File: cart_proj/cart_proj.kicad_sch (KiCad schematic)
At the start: 9 parts, among them CON1 GENESIS-EDGE, J1 PAD3, J2 PAD4, U1 PAL16R4, U2 74LS244, U3 74LS244, U4 27C800

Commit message: Add picture
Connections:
- net ~{XCVR2_OE}: now also U1.19 (IO1)
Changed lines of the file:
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@@
     (effects (font (size 1.27 1.27)) (justify left bottom))
+  )
+  (label "~{XCVR2_OE}" (at 82.55 26.67 180) (fields_autoplaced)
+    (effects (font (size 1.27 1.27)) (justify right bottom))
   )
   (label "A21" (at 278.13 64.77 180) (fields_autoplaced)

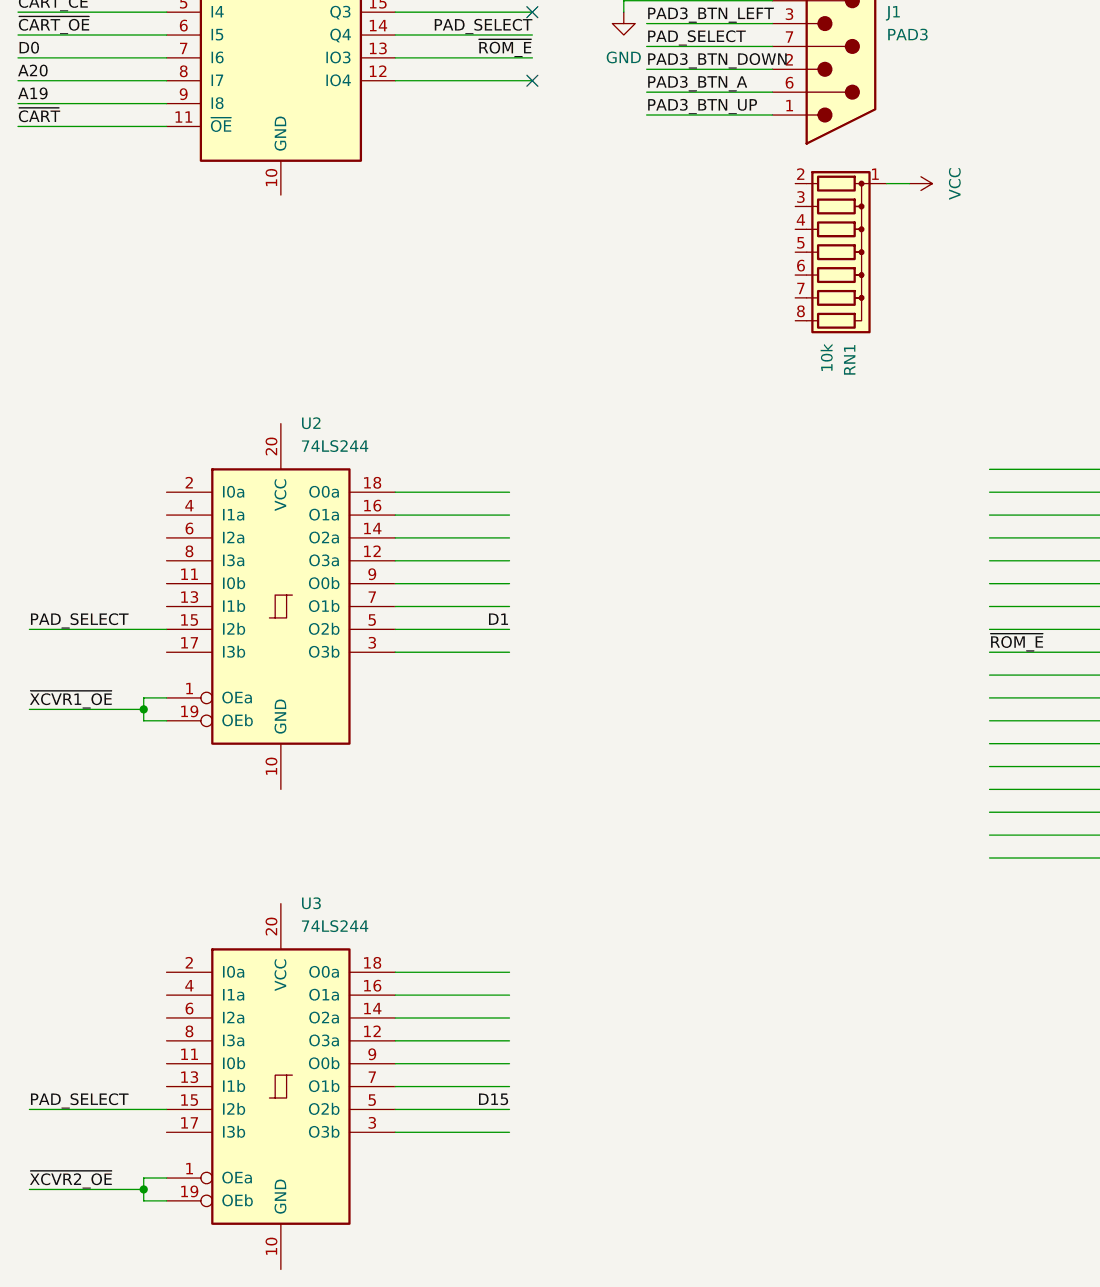
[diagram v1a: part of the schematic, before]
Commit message: Additional connections on first 74LS244
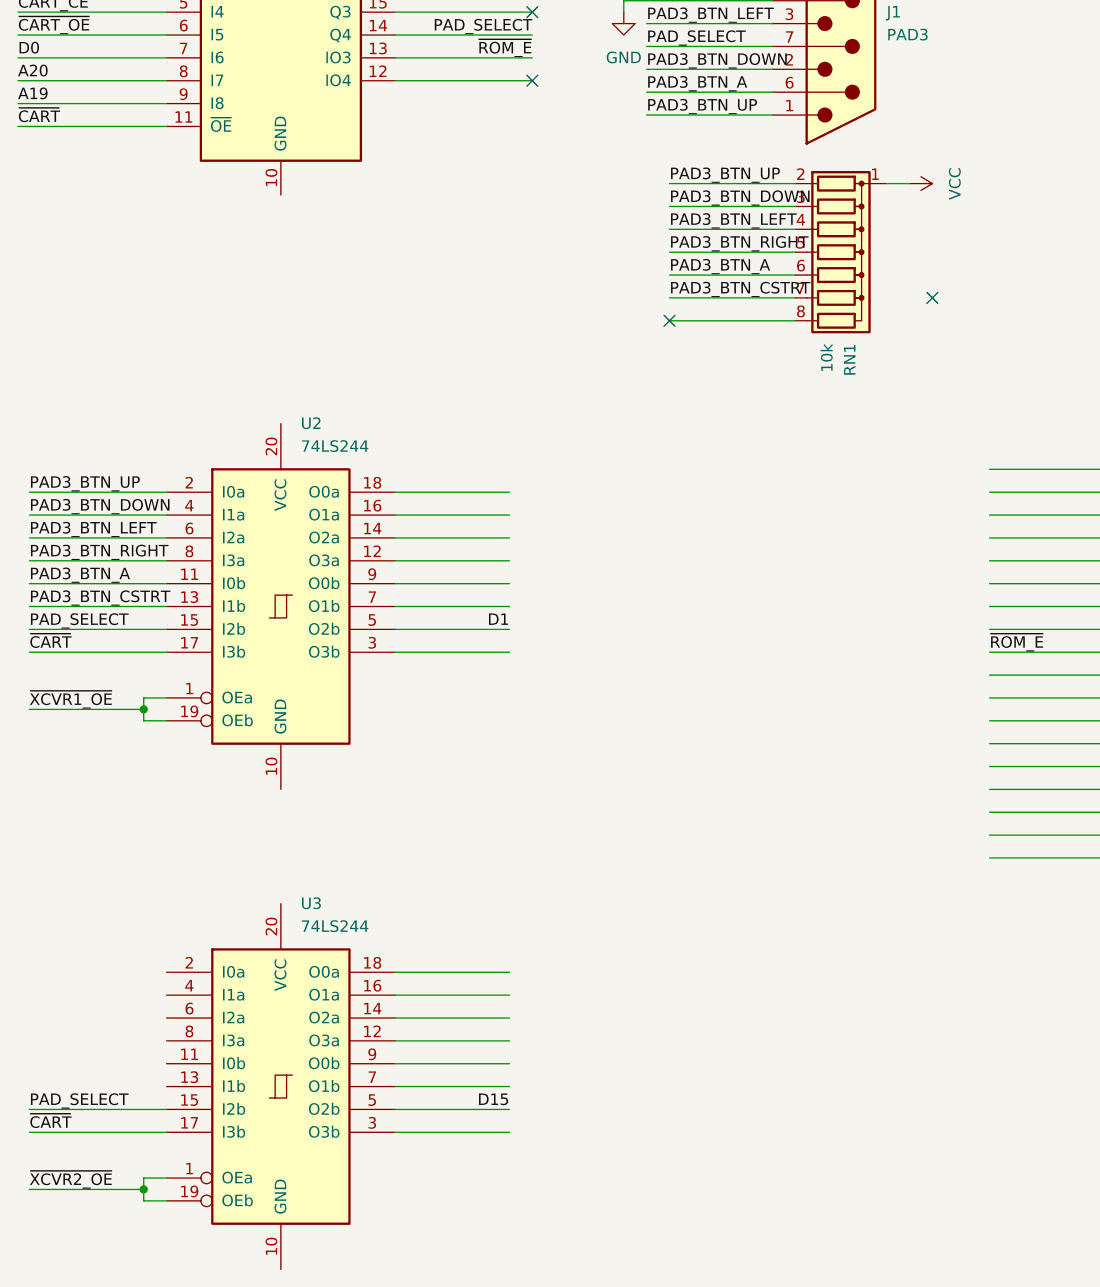
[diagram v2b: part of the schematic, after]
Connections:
- net PAD3_BTN_A: now also RN1.6 (R5), U2.11 (I0b)
- net PAD3_BTN_CSTRT: now also RN1.7 (R6), U2.13 (I1b)
- net PAD3_BTN_DOWN: now also RN1.3 (R2), U2.4 (I1a)
- net PAD3_BTN_LEFT: now also RN1.4 (R3), U2.6 (I2a)
- net PAD3_BTN_RIGHT: now also RN1.5 (R4), U2.8 (I3a)
- net PAD3_BTN_UP: now also RN1.2 (R1), U2.2 (I0a)
- net ~{CART}: now also U2.17 (I3b), U3.17 (I3b)
- no-connect marks 4 -> 6
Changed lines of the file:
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@@
   (junction (at 39.37 167.64) (diameter 0) (color 0 0 0 0)
   )
+  (no_connect (at 127 68.58))
   (no_connect (at 82.55 34.29))
   (no_connect (at 82.55 31.75))
   (no_connect (at 82.55 44.45))
+  (no_connect (at 97.79 71.12))
   (no_connect (at 82.55 36.83))
   (wire (pts (xy 95.25 33.02) (xy 109.22 33.02))
@@
     (stroke (width 0) (type default))
   )
+  (wire (pts (xy 26.67 100.33) (xy 41.91 100.33))
+    (stroke (width 0) (type default))
+  )
   (wire (pts (xy 67.31 41.91) (xy 82.55 41.91))
     (stroke (width 0) (type default))
@@
     (stroke (width 0) (type default))
   )
+  (wire (pts (xy 97.79 68.58) (xy 111.76 68.58))
+    (stroke (width 0) (type default))
+  )
   (wire (pts (xy 260.35 44.45) (xy 278.13 44.45))
     (stroke (width 0) (type default))
   )
+  (wire (pts (xy 26.67 95.25) (xy 41.91 95.25))
+    (stroke (width 0) (type default))
+  )
   (wire (pts (xy 260.35 49.53) (xy 278.13 49.53))
     (stroke (width 0) (type default))
@@
     (stroke (width 0) (type default))
   )
+  (wire (pts (xy 26.67 102.87) (xy 41.91 102.87))
+    (stroke (width 0) (type default))
+  )
   (wire (pts (xy 212.09 80.01) (xy 232.41 80.01))
     (stroke (width 0) (type default))
   )
+  (wire (pts (xy 97.79 60.96) (xy 111.76 60.96))
+    (stroke (width 0) (type default))
+  )
   (wire (pts (xy 92.71 27.94) (xy 109.22 27.94))
     (stroke (width 0) (type default))
@@
     (stroke (width 0) (type default))
   )
+  (wire (pts (xy 97.79 63.5) (xy 111.76 63.5))
+    (stroke (width 0) (type default))
+  )
   (wire (pts (xy 212.09 100.33) (xy 232.41 100.33))
     (stroke (width 0) (type default))
@@
     (stroke (width 0) (type default))
   )
+  (wire (pts (xy 97.79 66.04) (xy 111.76 66.04))
+    (stroke (width 0) (type default))
+  )
   (wire (pts (xy 41.91 105.41) (xy 26.67 105.41))
     (stroke (width 0) (type default))
@@
     (stroke (width 0) (type default))
   )
+  (wire (pts (xy 97.79 71.12) (xy 111.76 71.12))
+    (stroke (width 0) (type default))
+  )
+  (wire (pts (xy 26.67 90.17) (xy 41.91 90.17))
+    (stroke (width 0) (type default))
+  )
   (wire (pts (xy 67.31 31.75) (xy 82.55 31.75))
     (stroke (width 0) (type default))
@@
     (stroke (width 0) (type default))
   )
+  (wire (pts (xy 97.79 58.42) (xy 111.76 58.42))
+    (stroke (width 0) (type default))
+  )
+  (wire (pts (xy 97.79 55.88) (xy 111.76 55.88))
+    (stroke (width 0) (type default))
+  )
   (wire (pts (xy 133.35 92.71) (xy 149.86 92.71))
     (stroke (width 0) (type default))
@@
     (stroke (width 0) (type default))
   )
+  (wire (pts (xy 26.67 161.29) (xy 41.91 161.29))
+    (stroke (width 0) (type default))
+  )
   (wire (pts (xy 39.37 115.57) (xy 41.91 115.57))
     (stroke (width 0) (type default))
@@
     (stroke (width 0) (type default))
   )
+  (wire (pts (xy 26.67 92.71) (xy 41.91 92.71))
+    (stroke (width 0) (type default))
+  )
   (wire (pts (xy 133.35 125.73) (xy 149.86 125.73))
     (stroke (width 0) (type default))
@@
     (stroke (width 0) (type default))
   )
+  (wire (pts (xy 26.67 107.95) (xy 41.91 107.95))
+    (stroke (width 0) (type default))
+  )
   (wire (pts (xy 260.35 97.79) (xy 278.13 97.79))
     (stroke (width 0) (type default))
@@
     (stroke (width 0) (type default))
   )
+  (wire (pts (xy 26.67 97.79) (xy 41.91 97.79))
+    (stroke (width 0) (type default))
+  )
   (wire (pts (xy 260.35 110.49) (xy 278.13 110.49))
     (stroke (width 0) (type default))
@@
     (effects (font (size 1.27 1.27)) (justify left bottom))
   )
+  (label "PAD3_BTN_A" (at 97.79 66.04 0) (fields_autoplaced)
+    (effects (font (size 1.27 1.27)) (justify left bottom))
+  )
   (label "~{ROM_E}" (at 82.55 41.91 180) (fields_autoplaced)
     (effects (font (size 1.27 1.27)) (justify right bottom))
@@
     (effects (font (size 1.27 1.27)) (justify right bottom))
   )
+  (label "PAD3_BTN_LEFT" (at 97.79 60.96 0) (fields_autoplaced)
+    (effects (font (size 1.27 1.27)) (justify left bottom))
+  )
   (label "PAD4_BTN_UP" (at 154.94 48.26 0) (fields_autoplaced)
     (effects (font (size 1.27 1.27)) (justify left bottom))
@@
     (effects (font (size 1.27 1.27)) (justify left bottom))
   )
+  (label "PAD3_BTN_CSTRT" (at 97.79 68.58 0) (fields_autoplaced)
+    (effects (font (size 1.27 1.27)) (justify left bottom))
+  )
   (label "PAD4_BTN_A" (at 154.94 45.72 0) (fields_autoplaced)
     (effects (font (size 1.27 1.27)) (justify left bottom))
@@
     (effects (font (size 1.27 1.27)) (justify left bottom))
   )
+  (label "~{CART}" (at 26.67 107.95 0) (fields_autoplaced)
+    (effects (font (size 1.27 1.27)) (justify left bottom))
+  )
   (label "PAD4_BTN_DOWN" (at 154.94 43.18 0) (fields_autoplaced)
     (effects (font (size 1.27 1.27)) (justify left bottom))
@@
     (effects (font (size 1.27 1.27)) (justify right bottom))
   )
+  (label "PAD3_BTN_RIGHT" (at 26.67 97.79 0) (fields_autoplaced)
+    (effects (font (size 1.27 1.27)) (justify left bottom))
+  )
   (label "VCLK" (at 278.13 90.17 180) (fields_autoplaced)
     (effects (font (size 1.27 1.27)) (justify right bottom))
@@
     (effects (font (size 1.27 1.27)) (justify left bottom))
   )
+  (label "PAD3_BTN_DOWN" (at 26.67 92.71 0) (fields_autoplaced)
+    (effects (font (size 1.27 1.27)) (justify left bottom))
+  )
   (label "PAD3_BTN_DOWN" (at 95.25 43.18 0) (fields_autoplaced)
     (effects (font (size 1.27 1.27)) (justify left bottom))
   )
+  (label "PAD3_BTN_A" (at 26.67 100.33 0) (fields_autoplaced)
+    (effects (font (size 1.27 1.27)) (justify left bottom))
+  )
   (label "PAD3_BTN_LEFT" (at 95.25 38.1 0) (fields_autoplaced)
     (effects (font (size 1.27 1.27)) (justify left bottom))
@@
     (effects (font (size 1.27 1.27)) (justify right bottom))
   )
+  (label "PAD3_BTN_UP" (at 97.79 55.88 0) (fields_autoplaced)
+    (effects (font (size 1.27 1.27)) (justify left bottom))
+  )
+  (label "PAD3_BTN_UP" (at 26.67 90.17 0) (fields_autoplaced)
+    (effects (font (size 1.27 1.27)) (justify left bottom))
+  )
   (label "PAD_SELECT" (at 82.55 39.37 180) (fields_autoplaced)
     (effects (font (size 1.27 1.27)) (justify right bottom))
@@
     (effects (font (size 1.27 1.27)) (justify right bottom))
   )
+  (label "~{CART}" (at 26.67 161.29 0) (fields_autoplaced)
+    (effects (font (size 1.27 1.27)) (justify left bottom))
+  )
   (label "D1" (at 80.01 105.41 180) (fields_autoplaced)
     (effects (font (size 1.27 1.27)) (justify right bottom))
@@
     (effects (font (size 1.27 1.27)) (justify right bottom))
   )
+  (label "PAD3_BTN_CSTRT" (at 26.67 102.87 0) (fields_autoplaced)
+    (effects (font (size 1.27 1.27)) (justify left bottom))
+  )
   (label "~{ROM_E}" (at 133.35 107.95 0) (fields_autoplaced)
     (effects (font (size 1.27 1.27)) (justify left bottom))
@@
     (effects (font (size 1.27 1.27)) (justify left bottom))
   )
+  (label "PAD3_BTN_DOWN" (at 97.79 58.42 0) (fields_autoplaced)
+    (effects (font (size 1.27 1.27)) (justify left bottom))
+  )
   (label "A21" (at 25.4 34.29 0) (fields_autoplaced)
     (effects (font (size 1.27 1.27)) (justify left bottom))
@@
     (effects (font (size 1.27 1.27)) (justify left bottom))
   )
+  (label "PAD3_BTN_LEFT" (at 26.67 95.25 0) (fields_autoplaced)
+    (effects (font (size 1.27 1.27)) (justify left bottom))
+  )
   (label "A20" (at 278.13 62.23 180) (fields_autoplaced)
     (effects (font (size 1.27 1.27)) (justify right bottom))
@@
     (effects (font (size 1.27 1.27)) (justify left bottom))
   )
+  (label "PAD3_BTN_RIGHT" (at 97.79 63.5 0) (fields_autoplaced)
+    (effects (font (size 1.27 1.27)) (justify left bottom))
+  )

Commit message: Updated schematics
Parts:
- added C1: 100nF, symbol Device:C_Small
- added C2: 10uF, symbol Device:C_Polarized_Small
- U4: value 27C800 -> GAME ROM
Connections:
- net ~{CART} is gone; now on net GND: CON1.B32 (~{CART}), U1.11 (~{OE}), U2.17 (I3b), U3.17 (I3b)
- net D1: no longer U2.5 (O2b)
- net D15: now also U2.3 (O3b); no longer U3.5 (O2b)
- net GND: now also U1.10 (GND), U2.10 (GND), U3.10 (GND), C1.2, C2.2
- net PAD4_BTN_A: now also RN2.6 (R5)
- net PAD4_BTN_CSTRT: now also RN2.7 (R6)
- net PAD4_BTN_DOWN: now also RN2.3 (R2)
- net PAD4_BTN_LEFT: now also RN2.4 (R3)
- net PAD4_BTN_RIGHT: now also RN2.5 (R4)
- net PAD4_BTN_UP: now also RN2.2 (R1)
- net VCC: now also U1.20 (VCC), U2.20 (VCC), U3.20 (VCC), C1.1, C2.1
- net D13: now reaches U2.7 (O1b)
- net D13: now also CON1.B24 (D13)
- net D12: now reaches U2.9 (O0b)
- net D12: now also CON1.B25 (D12)
- net D7: now reaches CON1.A19 (D7)
- net D8: now reaches CON1.A21 (D8)
- net D6: now reaches CON1.A22 (D6)
- net D6: now also U3.5 (O2b)
- net D9: now reaches CON1.A24 (D9)
- net D5: now reaches CON1.A25 (D5)
- net D2: now reaches CON1.A26 (D2)
- net D10: now reaches CON1.A27 (D10)
- net D4: now reaches CON1.A28 (D4)
- net D3: now reaches CON1.A29 (D3)
- net D11: now reaches CON1.A30 (D11)
- net D14: now reaches CON1.B23 (D14)
- net D14: now also U2.5 (O2b)
- net A9: now reaches CON1.B4 (A9)
- net A10: now reaches CON1.B5 (A10)
- net A18: now reaches CON1.B6 (A18)
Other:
- moved on the sheet: U2, U3, U4

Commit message: Update schematics
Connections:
- net D10: now also U2.14 (O2a)
- net D11: now also U2.12 (O3a)
- net D8: now also U2.18 (O0a)
- net D9: now also U2.16 (O1a)
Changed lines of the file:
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@@
     (effects (font (size 1.27 1.27)) (justify left bottom))
+  )
+  (label "D11" (at 80.01 95.25 180) (fields_autoplaced)
+    (effects (font (size 1.27 1.27)) (justify right bottom))
   )
   (label "PAD3_BTN_CSTRT" (at 97.79 68.58 0) (fields_autoplaced)
@@
     (effects (font (size 1.27 1.27)) (justify left bottom))
   )
+  (label "D9" (at 80.01 90.17 180) (fields_autoplaced)
+    (effects (font (size 1.27 1.27)) (justify right bottom))
+  )
   (label "D9" (at 212.09 102.87 0) (fields_autoplaced)
     (effects (font (size 1.27 1.27)) (justify left bottom))
@@
     (effects (font (size 1.27 1.27)) (justify left bottom))
   )
+  (label "D8" (at 80.01 87.63 180) (fields_autoplaced)
+    (effects (font (size 1.27 1.27)) (justify right bottom))
+  )
   (label "~{CART_CE}" (at 25.4 36.83 0) (fields_autoplaced)
     (effects (font (size 1.27 1.27)) (justify left bottom))
   )
+  (label "D10" (at 80.01 92.71 180) (fields_autoplaced)
+    (effects (font (size 1.27 1.27)) (justify right bottom))
+  )
   (label "~{CART_OE}" (at 25.4 39.37 0) (fields_autoplaced)

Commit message: Update schematics
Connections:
- net D0: now also U4.14 (Q0)
- net D7: now also U3.3 (O3b)
- net PAD4_BTN_A: now also U3.11 (I0b)
- net PAD4_BTN_CSTRT: now also U3.13 (I1b)
- net PAD4_BTN_DOWN: now also U3.4 (I1a)
- net PAD4_BTN_LEFT: now also U3.6 (I2a)
- net PAD4_BTN_RIGHT: now also U3.8 (I3a)
- net PAD4_BTN_UP: now also U3.2 (I0a)
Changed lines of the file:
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@@
+    (stroke (width 0) (type default))
+  )
+  (wire (pts (xy 26.67 157.48) (xy 41.91 157.48))
     (stroke (width 0) (type default))
   )
@@
     (stroke (width 0) (type default))
   )
+  (wire (pts (xy 26.67 154.94) (xy 41.91 154.94))
+    (stroke (width 0) (type default))
+  )
   (wire (pts (xy 140.97 100.33) (xy 157.48 100.33))
     (stroke (width 0) (type default))
@@
     (stroke (width 0) (type default))
   )
+  (wire (pts (xy 26.67 152.4) (xy 41.91 152.4))
+    (stroke (width 0) (type default))
+  )
   (wire (pts (xy 140.97 135.89) (xy 157.48 135.89))
     (stroke (width 0) (type default))
@@
     (stroke (width 0) (type default))
   )
+  (wire (pts (xy 26.67 147.32) (xy 41.91 147.32))
+    (stroke (width 0) (type default))
+  )
   (wire (pts (xy 101.6 118.11) (xy 107.95 118.11))
     (stroke (width 0) (type default))
@@
     (stroke (width 0) (type default))
   )
+  (wire (pts (xy 26.67 160.02) (xy 41.91 160.02))
+    (stroke (width 0) (type default))
+  )
   (wire (pts (xy 140.97 140.97) (xy 157.48 140.97))
     (stroke (width 0) (type default))
@@
     (stroke (width 0) (type default))
   )
+  (wire (pts (xy 26.67 149.86) (xy 41.91 149.86))
+    (stroke (width 0) (type default))
+  )
   (wire (pts (xy 184.15 55.88) (xy 181.61 55.88))
     (stroke (width 0) (type default))
@@
     (effects (font (size 1.27 1.27)) (justify left bottom))
   )
+  (label "PAD4_BTN_CSTRT" (at 26.67 160.02 0) (fields_autoplaced)
+    (effects (font (size 1.27 1.27)) (justify left bottom))
+  )
   (label "PAD4_BTN_CSTRT" (at 154.94 30.48 0) (fields_autoplaced)
     (effects (font (size 1.27 1.27)) (justify left bottom))
@@
     (effects (font (size 1.27 1.27)) (justify right bottom))
   )
+  (label "PAD4_BTN_UP" (at 26.67 147.32 0) (fields_autoplaced)
+    (effects (font (size 1.27 1.27)) (justify left bottom))
+  )
   (label "PAD4_BTN_DOWN" (at 157.48 58.42 0) (fields_autoplaced)
     (effects (font (size 1.27 1.27)) (justify left bottom))
@@
     (effects (font (size 1.27 1.27)) (justify left bottom))
   )
+  (label "PAD4_BTN_LEFT" (at 26.67 152.4 0) (fields_autoplaced)
+    (effects (font (size 1.27 1.27)) (justify left bottom))
+  )
+  (label "PAD4_BTN_DOWN" (at 26.67 149.86 0) (fields_autoplaced)
+    (effects (font (size 1.27 1.27)) (justify left bottom))
+  )
   (label "D6" (at 80.01 162.56 180) (fields_autoplaced)
     (effects (font (size 1.27 1.27)) (justify right bottom))
@@
     (effects (font (size 1.27 1.27)) (justify right bottom))
   )
+  (label "D0" (at 140.97 123.19 0) (fields_autoplaced)
+    (effects (font (size 1.27 1.27)) (justify left bottom))
+  )
   (label "PAD3_BTN_UP" (at 97.79 55.88 0) (fields_autoplaced)
     (effects (font (size 1.27 1.27)) (justify left bottom))
@@
     (effects (font (size 1.27 1.27)) (justify left bottom))
   )
+  (label "PAD4_BTN_RIGHT" (at 26.67 154.94 0) (fields_autoplaced)
+    (effects (font (size 1.27 1.27)) (justify left bottom))
+  )
   (label "PAD3_BTN_UP" (at 26.67 87.63 0) (fields_autoplaced)
     (effects (font (size 1.27 1.27)) (justify left bottom))
@@
     (effects (font (size 1.27 1.27)) (justify left bottom))
   )
+  (label "PAD4_BTN_A" (at 26.67 157.48 0) (fields_autoplaced)
+    (effects (font (size 1.27 1.27)) (justify left bottom))
+  )
   (label "A22" (at 278.13 67.31 180) (fields_autoplaced)
     (effects (font (size 1.27 1.27)) (justify right bottom))
@@
     (effects (font (size 1.27 1.27)) (justify right bottom))
   )
+  (label "D7" (at 80.01 165.1 180) (fields_autoplaced)
+    (effects (font (size 1.27 1.27)) (justify right bottom))
+  )

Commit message: Update schematic
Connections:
- net D0: now also U3.18 (O0a)
- net D1: now also U3.16 (O1a)
- net D2: now also U3.14 (O2a)
- net D3: now also U3.12 (O3a)
- net D4: now also U3.9 (O0b)
- net D5: now also U3.7 (O1b)
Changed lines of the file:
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@@
+    (effects (font (size 1.27 1.27)) (justify right bottom))
+  )
+  (label "D3" (at 80.01 154.94 180) (fields_autoplaced)
     (effects (font (size 1.27 1.27)) (justify right bottom))
   )
@@
     (effects (font (size 1.27 1.27)) (justify left bottom))
   )
+  (label "D1" (at 80.01 149.86 180) (fields_autoplaced)
+    (effects (font (size 1.27 1.27)) (justify right bottom))
+  )
   (label "PAD4_BTN_DOWN" (at 157.48 58.42 0) (fields_autoplaced)
     (effects (font (size 1.27 1.27)) (justify left bottom))
@@
     (effects (font (size 1.27 1.27)) (justify right bottom))
   )
+  (label "D0" (at 80.01 147.32 180) (fields_autoplaced)
+    (effects (font (size 1.27 1.27)) (justify right bottom))
+  )
   (label "PAD3_BTN_LEFT" (at 97.79 60.96 0) (fields_autoplaced)
     (effects (font (size 1.27 1.27)) (justify left bottom))
@@
     (effects (font (size 1.27 1.27)) (justify right bottom))
   )
+  (label "D4" (at 80.01 157.48 180) (fields_autoplaced)
+    (effects (font (size 1.27 1.27)) (justify right bottom))
+  )
   (label "D7" (at 212.09 90.17 0) (fields_autoplaced)
     (effects (font (size 1.27 1.27)) (justify left bottom))
@@
     (effects (font (size 1.27 1.27)) (justify right bottom))
   )
+  (label "D2" (at 80.01 152.4 180) (fields_autoplaced)
+    (effects (font (size 1.27 1.27)) (justify right bottom))
+  )
   (label "A21" (at 278.13 64.77 180) (fields_autoplaced)
     (effects (font (size 1.27 1.27)) (justify right bottom))
@@
     (effects (font (size 1.27 1.27)) (justify right bottom))
   )
+  (label "D5" (at 80.01 160.02 180) (fields_autoplaced)
+    (effects (font (size 1.27 1.27)) (justify right bottom))
+  )
